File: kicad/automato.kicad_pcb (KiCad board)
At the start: 4 copper layers, 106 x 64 mm, 109 parts, among them J1 USB_C_Receptacle, J10 QWIIC 0, J12 STEMMA 0, J2 LiPo, J3 Conn_01x07_Male, J4 Screw_Terminal_01x14, J5 USB_C_Receptacle, J6 Conn_Coaxial, J7 1-WIRE, J8 Micro_SD_Card_Det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

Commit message: more route
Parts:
- moved D4 1.06 mm to (91.0, 109.8)
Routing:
- net VBUS: track 54.6 -> 118.3 mm, vias 4 -> 5
- net VBAT: track 2.75 -> 33.8 mm, vias 0 -> 2
- net Net-(D4-Pad1): track 0.00 -> 26.9 mm, vias 0 -> 2
- net EN: track 24.8 -> 47.8 mm, vias 0 -> 2
- net VIN: track 6.83 -> 21.7 mm, vias 0 -> 1
- net CS_RELAY: track 0.00 -> 13.4 mm, vias 0 -> 2
- net Net-(C14-Pad2): track 9.77 -> 20.4 mm
- net Net-(J6-Pad1): track 0.00 -> 8.22 mm
- net +3V3: track 46.7 -> 53.1 mm, vias 17 -> 21
- net RX: track 0.00 -> 1.46 mm, vias 0 -> 1
- net TX: track 0.00 -> 1.27 mm, vias 0 -> 1
- net GND: vias 29 -> 30

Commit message: routing
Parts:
- removed G***: LOGO, logo:SCL Symbol
- removed G***: LOGO, logo:VBAT
- removed G***: LOGO, logo:Positive Symbol
- removed G***: LOGO, logo:Wifi Logo
- removed G***: LOGO, logo:USB Symbol
- removed G***: LOGO, logo:Temp-Humidity_Box
- removed G***: LOGO, logo:Logo_Simple_Small_NoText
- removed G*** (x3): LOGO, logo:GND
- removed G***: LOGO, logo:ESP32__BubbleText
- removed G***: LOGO, logo:SDA Symbol
- removed G***: LOGO, logo:BlueTooth Logo
- removed G*** (x2): LOGO, logo:Automato_TextOnly_Small
- removed G***: LOGO, logo:Automato Logo Mixer_BOLD_Neg
- removed G***: LOGO, logo:Antenna
- removed G***: LOGO, logo:TX Symbol
- removed G***: LOGO, logo:RX Symbol
- removed G***: LOGO, logo:Battery Symbol_V2
- removed G***: LOGO, logo:USB_Symbol Only
- removed G***: LOGO, logo:VIN
- removed G***: LOGO, logo:VIN Voltage Range
- removed G***: LOGO, logo:VBAT Voltage Range
- removed REF** (x4): MountingHole_3.2mm_M3_Pad, MountingHole:MountingHole_3.2mm_M3_Pad
- added U8: ESP32-WROOM-DA, automato-sensor:ESP32-WROOM-DA, F.Cu at (211.5, 76.2)
- moved TP2 35.1 mm to (179.8, 61.2)
- moved TP1 34.2 mm to (177.2, 59.2)
- moved TP3 27.9 mm to (182.2, 63.2)
- moved C5 23.4 mm to (113.8, 80.3)
- moved R6 1.84 mm to (136.8, 73.3), turned to 270 degrees
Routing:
- net SPI_MOSI: track 0.00 -> 108.2 mm, vias 0 -> 4
- net SPI_CLK: track 0.00 -> 106.7 mm, vias 0 -> 4
- net BUSY_EINK: track 0.00 -> 59.0 mm, vias 0 -> 2
- net RST_EINK: track 0.00 -> 57.1 mm, vias 0 -> 2
- net DC_EINK: track 0.00 -> 54.9 mm, vias 0 -> 2
- net CS_EINK: track 0.00 -> 53.9 mm, vias 0 -> 2
- net SPI_MISO: track 0.00 -> 51.9 mm, vias 0 -> 2
- net IO15: track 10.5 -> 60.5 mm, vias 0 -> 1
- net IO16: track 16.3 -> 62.0 mm, vias 2 -> 3
- net Net-(J10-Pad4): track 6.80 -> 49.7 mm, vias 0 -> 2
- net Net-(J10-Pad3): track 2.94 -> 45.8 mm, vias 0 -> 2
- net Net-(J10-Pad2): track 3.52 -> 39.7 mm, vias 0 -> 2
- net CS_SD: track 0.00 -> 34.6 mm
- net Net-(J9-Pad3): track 2.89 -> 25.6 mm, vias 0 -> 2
- net Net-(J9-Pad4): track 6.45 -> 28.4 mm, vias 0 -> 2
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
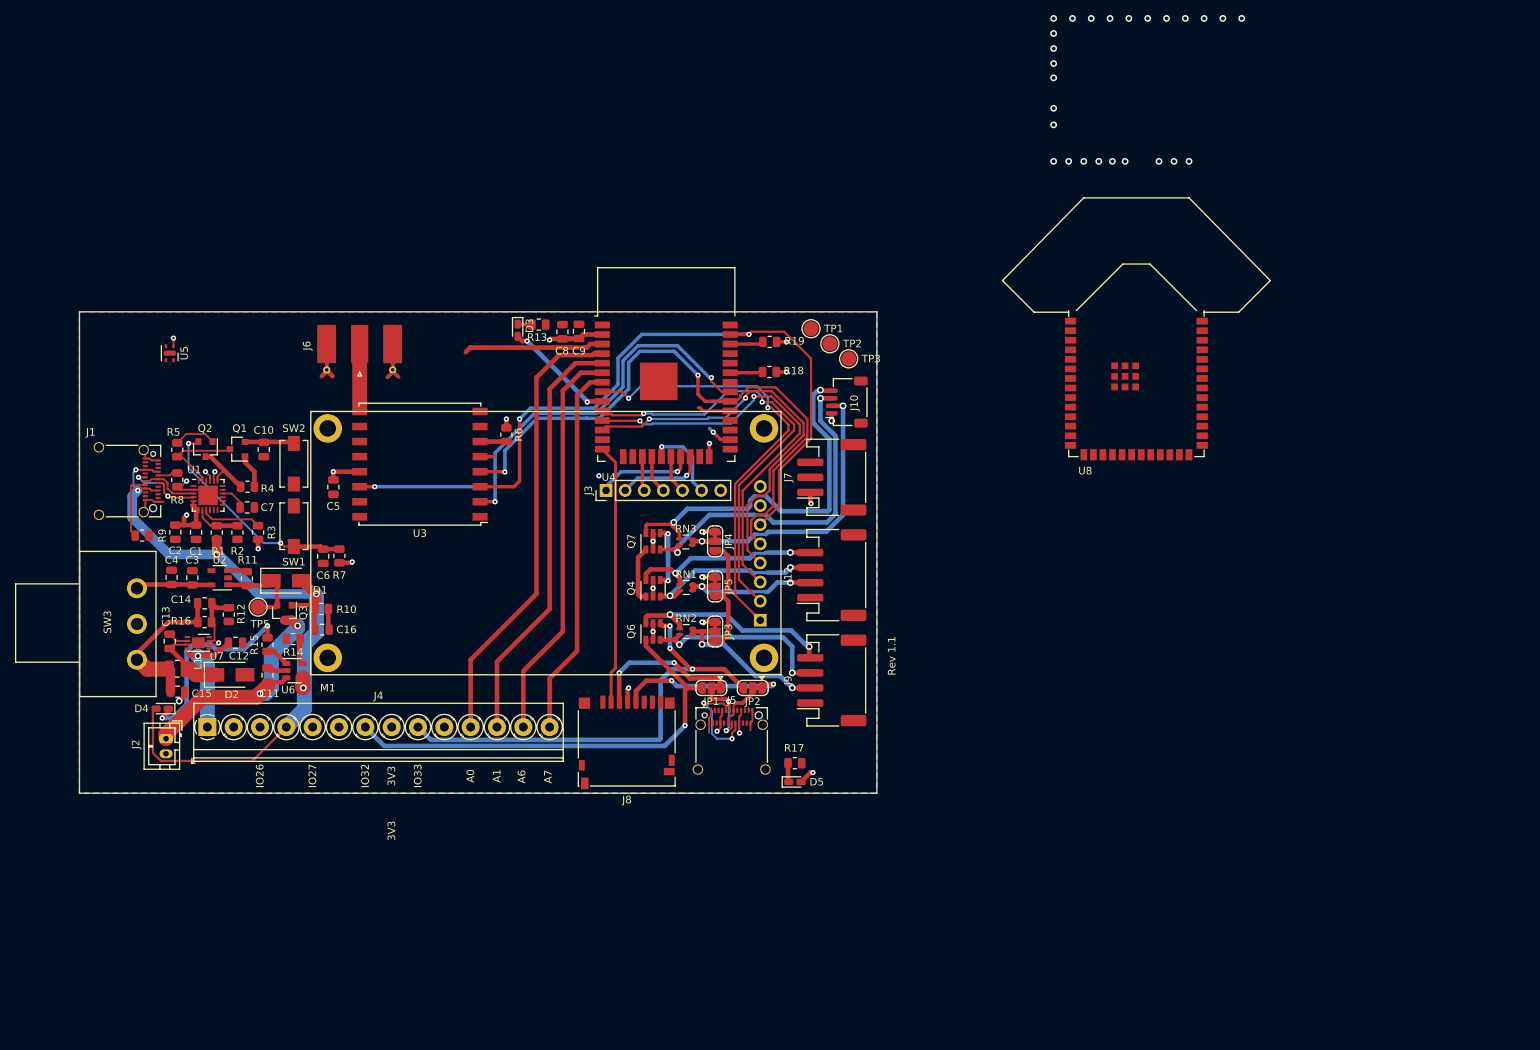
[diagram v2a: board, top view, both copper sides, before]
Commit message: put mounting holes back
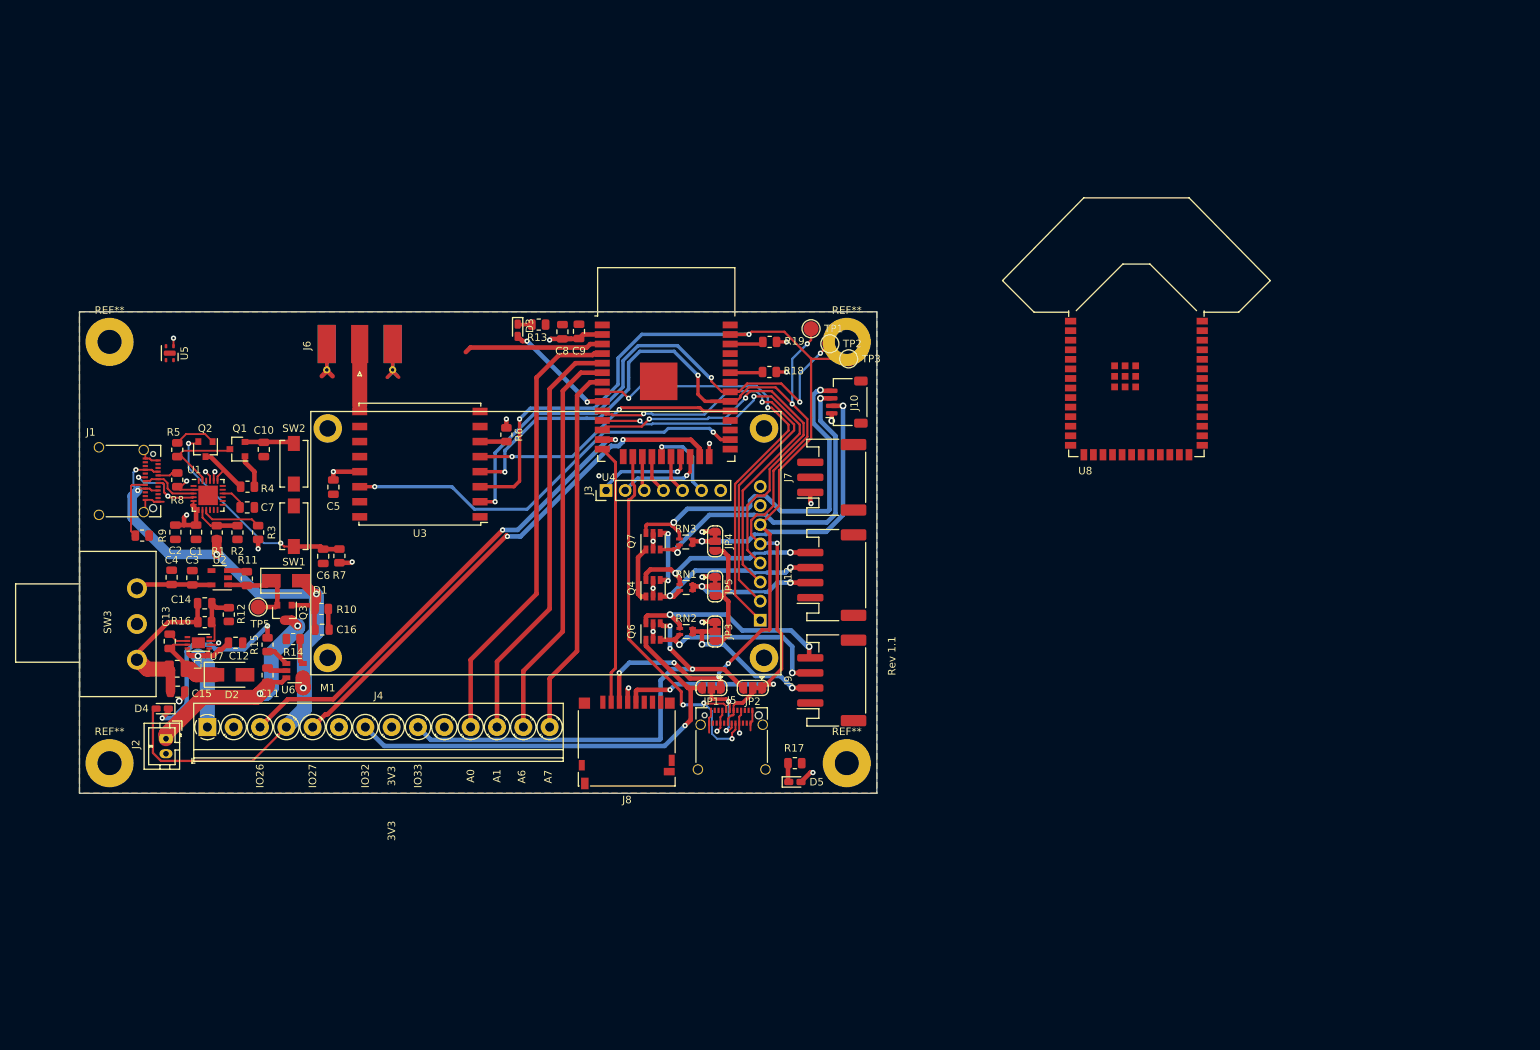
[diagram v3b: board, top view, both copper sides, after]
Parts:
- added REF**: MountingHole_3.2mm_M3_Pad, MountingHole:MountingHole_3.2mm_M3_Pad, F.Cu at (84.0, 117.0)
- added REF**: MountingHole_3.2mm_M3_Pad, MountingHole:MountingHole_3.2mm_M3_Pad, F.Cu at (84.0, 61.0)
- added REF**: MountingHole_3.2mm_M3_Pad, MountingHole:MountingHole_3.2mm_M3_Pad, F.Cu at (182.0, 61.0)
- added REF**: MountingHole_3.2mm_M3_Pad, MountingHole:MountingHole_3.2mm_M3_Pad, F.Cu at (182.0, 117.0)
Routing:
- net IO14: track 0.00 -> 69.1 mm, vias 0 -> 2
- net IO13: track 0.00 -> 64.8 mm, vias 0 -> 2
- net CS_RELAY: track 13.4 -> 52.9 mm, vias 2 -> 3
- net IRQ_LORA: track 18.6 -> 55.9 mm
- net SPI_CLK: track 106.7 -> 139.3 mm, vias 4 -> 7
- net CS_LORA: track 6.43 -> 36.4 mm, vias 0 -> 2
- net SPI_MOSI: track 108.2 -> 137.6 mm, vias 4 -> 6
- net SPI_MISO: track 51.9 -> 72.1 mm, vias 2 -> 4
- net GND: vias 31 -> 5

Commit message: routing
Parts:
- moved TP1 7.16 mm to (175.8, 66.2)
- moved TP2 5.39 mm to (174.8, 63.2)
- moved TP3 4.53 mm to (177.8, 63.8)
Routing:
- net VBUS: track 118.3 -> 173.6 mm, vias 5 -> 6
- net I2C_SDA: track 12.6 -> 67.7 mm, vias 2 -> 3
- net IO0: track 6.58 -> 59.9 mm
- net SPI_MISO: track 72.1 -> 125.1 mm
- net I2C_SCL: track 12.0 -> 60.8 mm, vias 0 -> 2
- net IO16: track 62.0 -> 106.2 mm, vias 3 -> 4
- net IO15: track 61.0 -> 103.6 mm
- net RX: track 1.46 -> 41.8 mm
- net TX: track 1.27 -> 40.8 mm
- net EN: track 47.8 -> 66.2 mm
- net RST_LORA: track 5.52 -> 18.2 mm, vias 1 -> 0
- net SPI_CLK: track 139.3 -> 131.5 mm, vias 7 -> 5
- net SPI_MOSI: track 137.6 -> 132.6 mm
- net GND: track 44.0 -> 47.7 mm, vias 5 -> 6

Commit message: writing in wroom-da
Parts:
- removed REF** (x4): MountingHole_3.2mm_M3_Pad, MountingHole:MountingHole_3.2mm_M3_Pad
- moved U8 23.8 mm to (189.5, 67.3)
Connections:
- D3 pad 2: Net-(D3-Pad2) -> IO14
- U4 pad 9: Net-(D3-Pad2) -> IO14
- U8 pad 1: Net-(U8-Pad1) -> GND
- U8 pad 11: Net-(U8-Pad11) -> DC_EINK
- U8 pad 12: Net-(U8-Pad12) -> CS_EINK
- U8 pad 13: Net-(U8-Pad13) -> IO14
- U8 pad 14: Net-(U8-Pad14) -> CS_RELAY
- U8 pad 16: Net-(U8-Pad16) -> GND
- U8 pad 17: Net-(U8-Pad17) -> IO13
- U8 pad 2: Net-(U8-Pad2) -> +3V3
- U8 pad 24: Net-(U8-Pad24) -> IO15
- U8 pad 27: Net-(U8-Pad27) -> IO0
- U8 pad 28: Net-(U8-Pad28) -> CS_LORA
- U8 pad 29: Net-(U8-Pad29) -> IO16
- U8 pad 3: Net-(U8-Pad3) -> EN
- U8 pad 30: Net-(U8-Pad30) -> SPI_CLK
- U8 pad 31: Net-(U8-Pad31) -> CS_SD
- U8 pad 32: Net-(U8-Pad32) -> SPI_MISO
- U8 pad 33: Net-(U8-Pad33) -> I2C_SDA
- U8 pad 35: Net-(U8-Pad35) -> I2C_SCL
- U8 pad 36: Net-(U8-Pad36) -> RX
- U8 pad 37: Net-(U8-Pad37) -> TX
- U8 pad 38: Net-(U8-Pad38) -> SPI_MOSI
- U8 pad 39: Net-(U8-Pad39) -> RST_EINK
- U8 pad 4: Net-(U8-Pad4) -> A0
- U8 pad 40: Net-(U8-Pad40) -> GND
- U8 pad 43: Net-(U8-Pad43) -> GND
- U8 pad 5: Net-(U8-Pad5) -> A1
- U8 pad 6: Net-(U8-Pad6) -> A6
- U8 pad 7: Net-(U8-Pad7) -> A7
- U8 pad 8: Net-(U8-Pad8) -> BUSY_EINK
- U8 pad 9: Net-(U8-Pad9) -> IRQ_LORA
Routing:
- net Net-(D3-Pad2): track 15.0 -> 0.00 mm, vias 2 -> 0
- net IO14: track 69.1 -> 84.1 mm, vias 2 -> 4
- net I2C_SDA: track 67.7 -> 61.1 mm
- net I2C_SCL: track 60.8 -> 55.2 mm
- net Net-(J10-Pad3): track 45.8 -> 46.8 mm
- net Net-(J10-Pad4): track 49.7 -> 49.1 mm
- net Net-(J12-Pad3): track 24.0 -> 24.5 mm

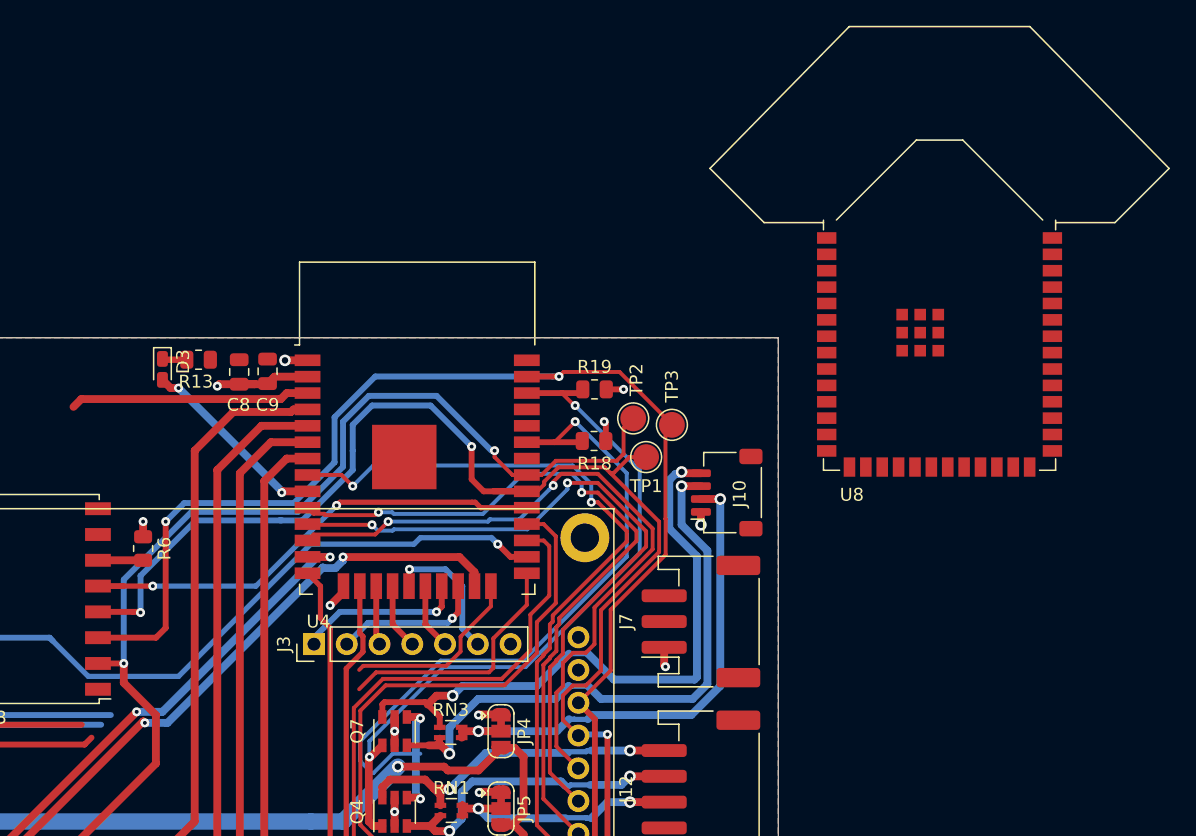
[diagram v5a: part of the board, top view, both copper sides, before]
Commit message: swap in wroom-da, remove swd header
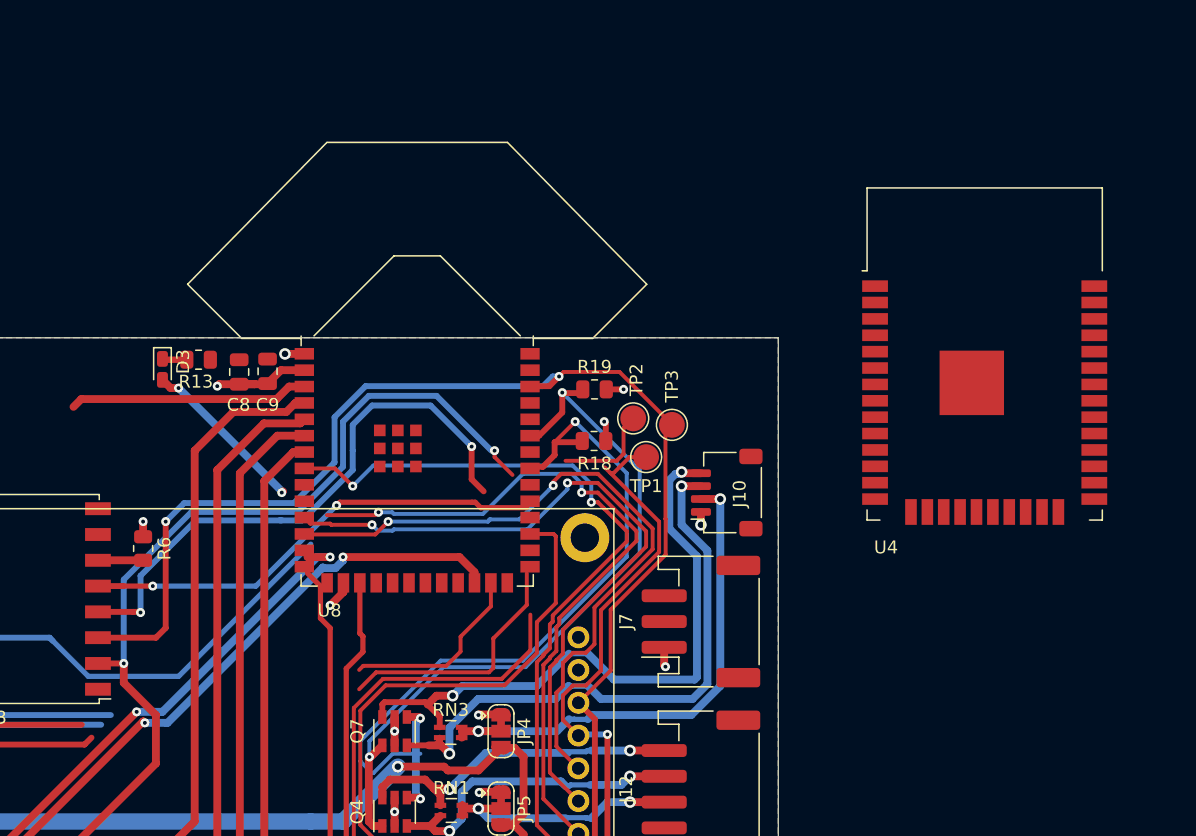
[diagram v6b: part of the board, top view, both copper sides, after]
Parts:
- removed J3: Conn_01x07_Male, Connector_PinHeader_2.54mm:PinHeader_1x07_P2.54mm_Vertical
- moved U4 44.4 mm to (202.0, 61.2)
- moved U8 41.5 mm to (149.0, 76.2)
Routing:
- net IRQ_LORA: track 55.9 -> 38.3 mm, vias 2 -> 1
- net RST_LORA: track 18.2 -> 3.75 mm
- net (no net): track 0.00 -> 14.5 mm
- net SPI_CLK: track 131.5 -> 118.6 mm
- net Net-(J3-Pad1): track 12.7 -> 0.00 mm, vias 1 -> 0
- net Net-(J3-Pad2): track 11.4 -> 0.00 mm, vias 1 -> 0
- net Net-(J3-Pad6): track 11.2 -> 0.00 mm, vias 1 -> 0
- net IO15: track 103.3 -> 95.5 mm
- net Net-(J3-Pad5): track 4.88 -> 0.00 mm
- net Net-(J3-Pad4): track 4.88 -> 0.00 mm
- net SPI_MISO: track 125.1 -> 120.5 mm
- net Net-(J3-Pad3): track 4.35 -> 0.00 mm
- net I2C_SCL: track 55.2 -> 57.3 mm
- net IO14: track 84.1 -> 82.2 mm
- net RST_EINK: track 57.0 -> 55.3 mm
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
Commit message: finished routing
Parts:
- removed U4: ESP32-WROOM-32D, RF_Module:ESP32-WROOM-32
- added REF**: MountingHole_3.2mm_M3_DIN965_Pad_TopBottom, MountingHole:MountingHole_3.2mm_M3_DIN965_Pad_TopBottom, F.Cu at (83.1, 117.9)
- added REF**: MountingHole_3.2mm_M3_DIN965_Pad_TopBottom, MountingHole:MountingHole_3.2mm_M3_DIN965_Pad_TopBottom, F.Cu at (182.9, 117.9)
- added REF**: MountingHole_3.2mm_M3_DIN965_Pad_TopBottom, MountingHole:MountingHole_3.2mm_M3_DIN965_Pad_TopBottom, F.Cu at (182.9, 60.1)
- added REF**: MountingHole_3.2mm_M3_DIN965_Pad_TopBottom, MountingHole:MountingHole_3.2mm_M3_DIN965_Pad_TopBottom, F.Cu at (83.2, 60.1)
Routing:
- net I2C_SCL: track 57.3 -> 139.1 mm, vias 2 -> 6
- net I2C_SDA: track 62.3 -> 142.3 mm, vias 3 -> 6
- net RX: track 41.8 -> 86.2 mm, vias 1 -> 2
- net TX: track 40.8 -> 84.4 mm, vias 1 -> 2
- net IO0: track 59.9 -> 87.5 mm, vias 0 -> 2
- net EN: track 66.2 -> 88.3 mm, vias 2 -> 4
- net CS_SD: track 34.6 -> 50.3 mm, vias 0 -> 2
- net (no net): track 14.5 -> 0.00 mm
- net RST_EINK: track 55.3 -> 44.6 mm
- net SPI_MISO: track 120.5 -> 113.8 mm
- net IO15: track 95.5 -> 101.9 mm, vias 1 -> 3
- net GND: track 47.7 -> 53.7 mm, vias 6 -> 7
- net IO14: track 82.2 -> 85.5 mm
- net SPI_CLK: track 118.6 -> 121.4 mm
- net CS_RELAY: track 53.3 -> 55.5 mm
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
